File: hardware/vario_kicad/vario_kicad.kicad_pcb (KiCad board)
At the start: 2 copper layers, 70 x 50 mm, 94 parts, among them Q1 NMOS, Q2 PMOS, U2 BME280, U3 W25Q128JVS, U4 USB C connector, U5 STM32L072CBTx, Y1 Crystal, Y2 Crystal_GND24

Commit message: routing progress
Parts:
- R15, R4: moved to B.Cu
- moved C12 15.1 mm to (124.2, 135.8), turned to 180 degrees
- moved R26 12.8 mm to (124.1, 137.3), turned to 0 degrees
- moved C21 6.50 mm to (106.3, 139.9), turned to 180 degrees
- moved R15 2.86 mm to (113.0, 122.7)
- moved R4 2.02 mm to (112.5, 126.5)
- moved Y1 1.24 mm to (124.1, 130.3)
- moved C27 1.24 mm to (122.2, 128.9), turned to 90 degrees
- moved C26 1.11 mm to (122.2, 131.9), turned to -90 degrees
- moved R32 1.01 mm to (160.0, 135.2), turned to 180 degrees
- moved C13 0.06 mm to (133.2, 136.5)
- turned JP3 to 180 degrees
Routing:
- net V_USB: track 0.00 -> 78.4 mm, vias 0 -> 2
- net /mcu/NRST: track 0.00 -> 29.4 mm
- net /mcu/BOOT0: track 0.00 -> 22.6 mm
- net VBATT: track 0.00 -> 17.7 mm
- net /mcu/USB_D+: track 3.84 -> 18.4 mm
- net /mcu/USB_D-: track 3.36 -> 17.9 mm
- net /mcu/SWCLK: track 0.00 -> 13.5 mm
- net /mcu/SWDIO: track 0.00 -> 12.0 mm
- net VBATT_SW: track 0.00 -> 8.67 mm
- net Net-(U1-VoP): track 0.00 -> 8.33 mm
- net Net-(U1-VoN): track 0.00 -> 7.51 mm
- net Net-(Q1-D): track 0.00 -> 6.10 mm
- net /mcu/OSC32_OUT: track 0.00 -> 5.86 mm, vias 0 -> 1
- net /mcu/OSC32_IN: track 0.00 -> 5.61 mm, vias 0 -> 1
- net Net-(U4-CC1): track 0.03 -> 5.56 mm, vias 0 -> 1
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
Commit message: layout close to finished
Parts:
- C22: moved to B.Cu
- Y2: footprint Crystal:Crystal_SMD_3225-4Pin_3.2x2.5mm_HandSoldering -> Crystal:Crystal_SMD_3225-4Pin_3.2x2.5mm
- moved TP4 20.4 mm to (129.8, 137.8)
- moved D5 13.2 mm to (159.7, 135.4), turned to -90 degrees
- moved R28 12.9 mm to (158.2, 135.4), turned to -90 degrees
- moved C2 7.43 mm to (116.0, 111.1), turned to 90 degrees
- moved Q2 4.98 mm to (158.3, 127.1)
- moved R22 4.98 mm to (162.8, 126.1)
- moved R24 4.51 mm to (151.8, 127.7), turned to -90 degrees
- moved Q1 4.26 mm to (158.3, 131.7)
- moved R23 4.26 mm to (154.3, 131.7)
- moved R2 3.91 mm to (115.3, 117.0), turned to 180 degrees
- moved R25 3.55 mm to (149.8, 127.7)
- moved C1 2.91 mm to (110.9, 111.1), turned to 90 degrees
- moved R3 1.90 mm to (121.5, 112.0)
- moved C8 1.80 mm to (147.4, 114.6), turned to 180 degrees
- moved R5 1.40 mm to (121.4, 113.6)
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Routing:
- net VCC: track 3.17 -> 166.7 mm, vias 0 -> 12
- net GND: track 11.0 -> 77.4 mm, vias 0 -> 13
- net /mcu/SW3: track 0.00 -> 41.4 mm, vias 0 -> 2
- net /audio_amp/AUDIO_AMP_ENABLE: track 0.00 -> 34.0 mm, vias 0 -> 1
- net /mcu/MEM_CS_ALT: track 0.00 -> 31.9 mm, vias 0 -> 2
- net /leds/LED1: track 0.00 -> 29.8 mm
- net /leds/LED2: track 0.00 -> 27.3 mm
- net /mcu/ADC_IN3: track 0.00 -> 27.3 mm, vias 0 -> 1
- net /mcu/SPI1_NSS: track 0.00 -> 27.2 mm, vias 0 -> 2
- net /mcu/WKUP1: track 0.00 -> 26.5 mm
- net /leds/LED3: track 0.00 -> 24.9 mm
- net /bme280/BME280_I2C_SDA: track 0.00 -> 21.0 mm
- net /bme280/BME280_I2C_SCK: track 0.00 -> 20.7 mm, vias 0 -> 2
- net /mcu/SPI1_SCK: track 0.00 -> 18.8 mm
- net /mcu/MEM_HOLD: track 0.00 -> 18.7 mm, vias 0 -> 2
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- added copper zone on B.Cu, net GND

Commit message: layout&routing close to done
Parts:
- added C30: 100nF, Capacitor_SMD:C_0402_1005Metric, F.Cu at (128.5, 123.5)
- moved C12 15.2 mm to (112.0, 144.8), turned to -90 degrees
- moved R26 12.9 mm to (113.6, 144.8), turned to 90 degrees
- moved C1 3.30 mm to (107.6, 110.7)
- moved R1 3.30 mm to (107.0, 116.5)
- moved C2 3.30 mm to (112.8, 110.7)
- moved R2 3.30 mm to (112.0, 116.5)
- moved U2 3.30 mm to (110.2, 112.2)
- moved C29 1.03 mm to (116.0, 132.8)
- moved C25 0.94 mm to (130.8, 128.6)
- moved C11 0.94 mm to (132.2, 128.6)
- moved LS1 0.81 mm to (152.4, 115.5)
- moved C22 0.27 mm to (120.7, 122.0)
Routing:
- net /mcu/VBATT_SW_EN: track 0.00 -> 62.1 mm, vias 0 -> 1
- net VCC: track 166.7 -> 214.3 mm, vias 12 -> 14
- net /mcu/BOOT0: track 23.9 -> 4.57 mm
- net GND: track 77.4 -> 88.4 mm, vias 13 -> 20
- net VBATT: track 21.4 -> 28.5 mm
- net /mcu/SPI1_MOSI: track 16.3 -> 19.2 mm
- net Net-(JP3-A): track 3.59 -> 6.42 mm
- net /mcu/SPI1_NSS: track 27.2 -> 25.4 mm
- net /mcu/ADC_IN3: track 27.3 -> 29.1 mm, vias 1 -> 3
- net /bme280/BME280_I2C_SDA: track 21.0 -> 22.7 mm
- net /mcu/MEM_CS_ALT: track 31.9 -> 33.3 mm
- net /bme280/BME280_I2C_SCK: track 20.7 -> 22.1 mm
- net /mcu/SW3: track 41.4 -> 40.1 mm
- net Net-(U1-VoN): track 7.51 -> 8.56 mm
- net /mcu/MEM_WP: track 16.7 -> 17.7 mm
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- added copper zone on F.Cu, net GND

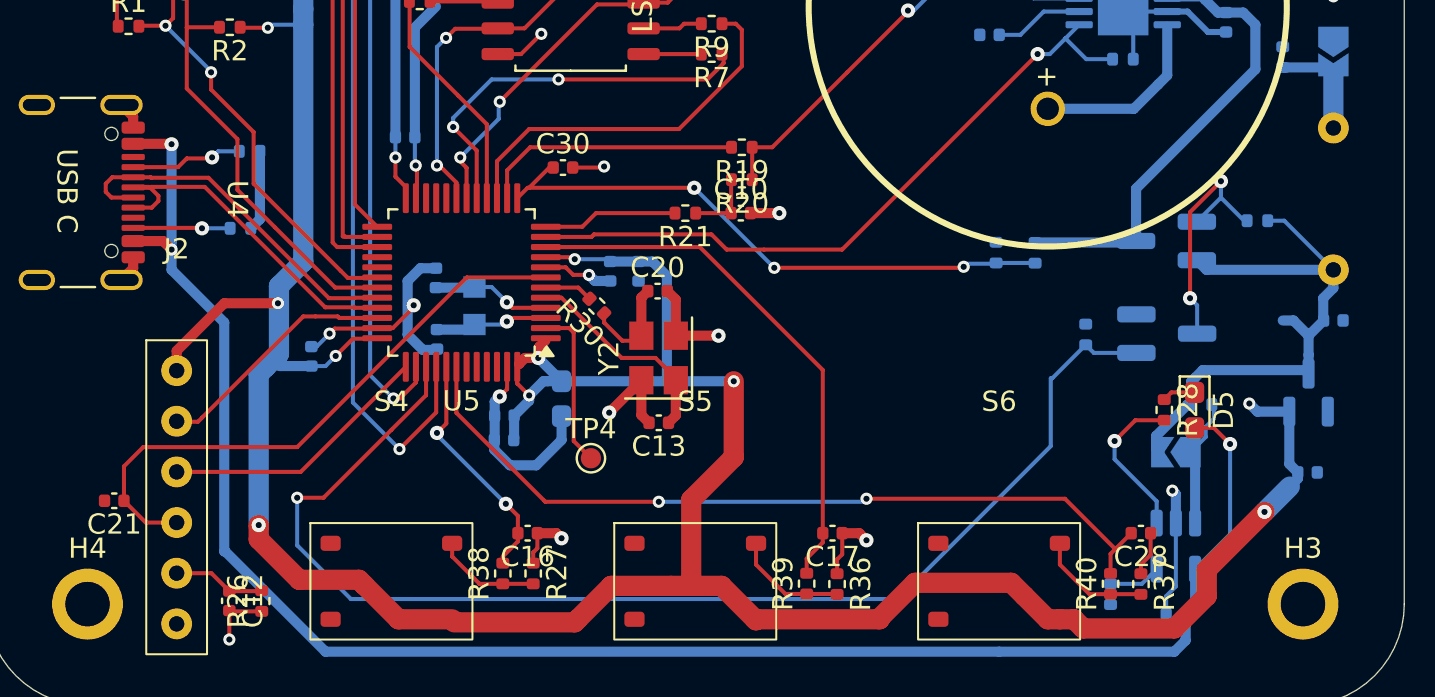
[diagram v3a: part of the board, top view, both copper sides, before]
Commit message: update usb c footprint for drc
shrink the usb c footprint pads closest to the NPTH mounting holes to
satisfy the DRC min distance 0.2mm hole to copper
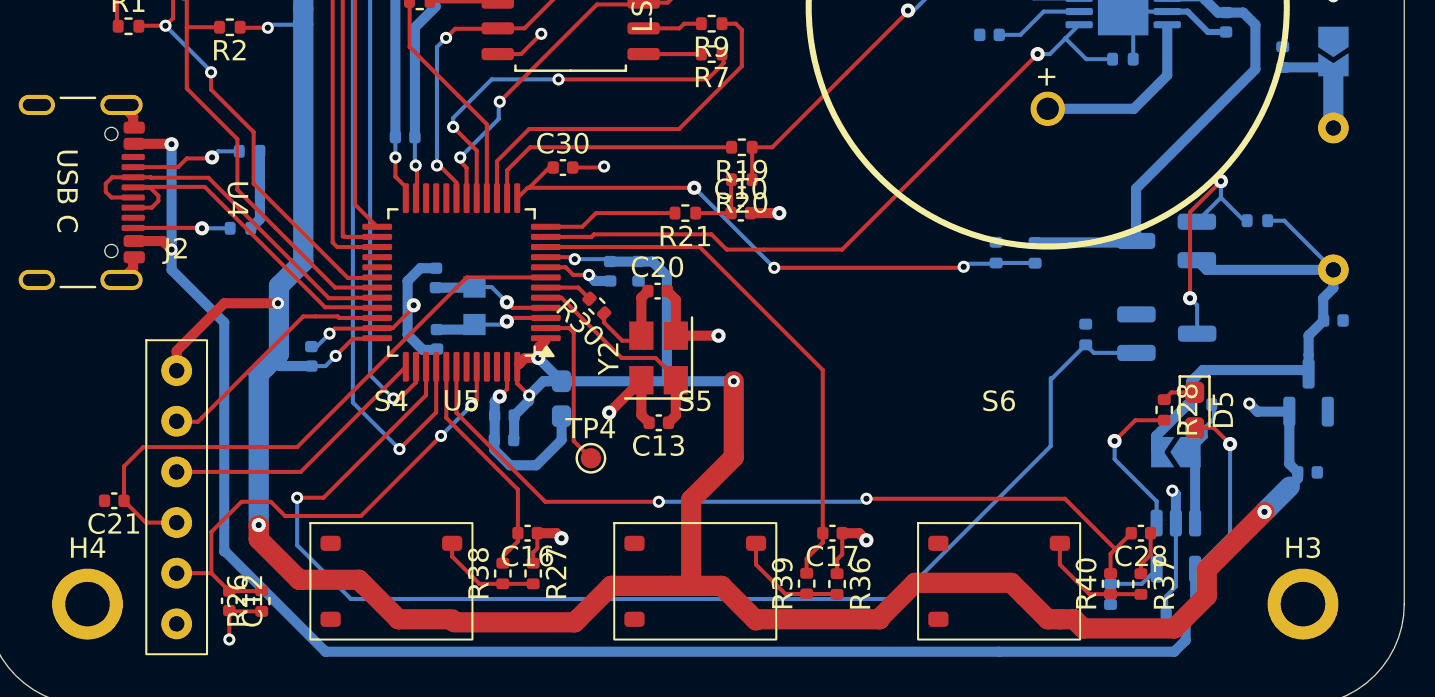
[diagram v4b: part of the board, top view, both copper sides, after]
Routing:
- net /mcu/BOOT0: track 4.57 -> 24.6 mm, vias 0 -> 2
- net VBATT: track 28.5 -> 26.9 mm
- net /mcu/SW1: track 11.8 -> 11.5 mm, vias 2 -> 0

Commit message: updates to layout v2
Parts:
- removed JP3: SolderJumper_2_Bridged, Jumper:SolderJumper-2_P1.3mm_Open_TrianglePad1.0x1.5mm
- BT2, C11, C22, C23, C24, C25, C29, C4, C8, C9, JP2, R15, R17, R18, R31, R4: moved to F.Cu
- C16, C17, C28, R27, R28, R36, R37, R38, R39, R40: moved to B.Cu
- moved R17 114.3 mm to (53.9, 53.9), turned to 0 degrees
- moved R18 112.5 mm to (53.9, 55.9), turned to 0 degrees
- moved R19 105.5 mm to (53.9, 57.8), turned to 0 degrees
- moved R20 105.3 mm to (53.9, 59.8), turned to 0 degrees
- moved C8 103.7 mm to (53.9, 69.7), turned to 0 degrees
- moved R21 102.9 mm to (53.9, 61.8), turned to 0 degrees
- moved C9 102.0 mm to (53.9, 71.7), turned to 0 degrees
- moved R26 101.0 mm to (74.2, 51.9), turned to 0 degrees
- moved TP4 98.9 mm to (58.9, 69.0)
- moved C10 98.3 mm to (53.9, 73.7)
- moved C11 95.3 mm to (62.9, 63.2), turned to 0 degrees
- moved C12 93.6 mm to (62.9, 65.2), turned to 0 degrees
- moved C23 92.5 mm to (65.8, 65.2), turned to 0 degrees
- moved C24 91.9 mm to (65.8, 67.2), turned to 0 degrees
- moved C25 88.1 mm to (65.8, 69.1), turned to 0 degrees
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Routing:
- net VCC: track 214.3 -> 7.95 mm, vias 14 -> 0
- net V_USB: track 87.6 -> 0.00 mm, vias 3 -> 0
- net GND: track 88.4 -> 5.75 mm, vias 20 -> 0
- net /mcu/VBATT_SW_EN: track 62.1 -> 0.00 mm, vias 1 -> 0
- net /mcu/SW3: track 40.1 -> 0.00 mm, vias 2 -> 0
- net /audio_amp/AUDIO_AMP_ENABLE: track 34.0 -> 0.00 mm, vias 1 -> 0
- net /mcu/MEM_CS_ALT: track 33.3 -> 0.00 mm, vias 2 -> 0
- net /leds/LED1: track 29.8 -> 0.00 mm
- net /mcu/NRST: track 29.4 -> 0.00 mm
- net /mcu/ADC_IN3: track 29.1 -> 0.00 mm, vias 3 -> 0
- net /leds/LED2: track 27.3 -> 0.00 mm
- net /mcu/WKUP1: track 26.5 -> 0.00 mm
- net /mcu/SPI1_NSS: track 25.4 -> 0.00 mm, vias 2 -> 0
- net /leds/LED3: track 24.9 -> 0.00 mm
- net /mcu/BOOT0: track 24.6 -> 0.00 mm, vias 2 -> 0
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
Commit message: update layout v2
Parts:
- C21, C23, C9, JP2, R18, R31: moved to B.Cu
- moved R17 111.4 mm to (139.1, 125.7), turned to 180 degrees
- moved R18 106.6 mm to (143.3, 114.0), turned to 180 degrees
- moved R19 104.0 mm to (135.5, 122.4), turned to 180 degrees
- moved R20 103.8 mm to (135.5, 124.0), turned to 180 degrees
- moved TP4 100.7 mm to (132.5, 137.7)
- moved C8 100.3 mm to (138.1, 124.1), turned to 180 degrees
- moved R21 99.8 mm to (131.9, 124.1), turned to 180 degrees
- moved C22 97.1 mm to (128.9, 136.9), turned to -90 degrees
- moved C11 96.8 mm to (131.9, 131.1), turned to -90 degrees
- moved C9 96.7 mm to (140.8, 114.0), turned to 180 degrees
- moved C10 95.3 mm to (133.6, 125.8), turned to -90 degrees
- moved C24 93.6 mm to (125.4, 139.3), turned to 180 degrees
- moved C25 89.3 mm to (130.1, 131.1), turned to -90 degrees
- moved C21 86.3 mm to (125.3, 130.7)
- moved C29 85.3 mm to (115.9, 136.2), turned to 135 degrees
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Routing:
- net VCC: track 7.95 -> 266.4 mm, vias 0 -> 11
- net V_USB: track 0.00 -> 100.5 mm, vias 0 -> 3
- net /leds/LED1: track 0.00 -> 41.8 mm
- net /leds/LED2: track 0.00 -> 38.9 mm
- net /mcu/MEM_CS_ALT: track 0.00 -> 37.1 mm, vias 0 -> 2
- net /leds/LED3: track 0.00 -> 35.9 mm
- net /audio_amp/AUDIO_AMP_ENABLE: track 0.00 -> 34.6 mm, vias 0 -> 1
- net /mcu/SW3: track 0.00 -> 33.4 mm, vias 0 -> 3
- net /mcu/VBATT_SW_EN: track 0.00 -> 33.3 mm, vias 0 -> 1
- net /mcu/SPI1_NSS: track 0.00 -> 31.7 mm, vias 0 -> 2
- net /bme280/BME280_I2C_SDA: track 0.00 -> 30.0 mm
- net VBATT_SW: track 0.00 -> 29.7 mm
- net GND: track 5.75 -> 35.3 mm, vias 0 -> 3
- net /bme280/BME280_I2C_SCK: track 0.00 -> 28.4 mm
- net /mcu/NRST: track 0.00 -> 25.0 mm, vias 0 -> 3
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
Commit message: almost finish 4layer board
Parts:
- removed C12: 100nF, Capacitor_SMD:C_0402_1005Metric
- C16, C17, C21, C23, C26, C27, C28, Q1, Q2, R22, R23, R24, R25, R27, R36, R37, R38, R39, R40, Y1: moved to F.Cu
- moved R26 100.4 mm to (114.5, 143.8), turned to 135 degrees
- moved C4 87.6 mm to (128.3, 138.0)
- moved C21 15.5 mm to (114.0, 141.3), turned to -45 degrees
- moved C27 14.4 mm to (133.4, 138.5), turned to -90 degrees
- moved R7 13.5 mm to (123.0, 125.8), turned to 90 degrees
- moved R9 13.5 mm to (124.5, 125.8), turned to 90 degrees
- moved R23 12.9 mm to (161.7, 138.0)
- moved C26 12.0 mm to (131.6, 138.5), turned to -90 degrees
- moved Y1 10.3 mm to (132.5, 136.2), turned to 180 degrees
- moved TP4 10.0 mm to (142.4, 139.2)
- moved C28 8.97 mm to (154.8, 143.0), turned to 90 degrees
- moved C17 8.61 mm to (141.8, 143.8), turned to 90 degrees
- moved R22 8.59 mm to (161.7, 133.9), turned to 90 degrees
- moved C16 8.01 mm to (129.3, 143.5), turned to 90 degrees
- moved R25 7.66 mm to (152.0, 130.9)
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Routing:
- net VCC: track 266.4 -> 49.2 mm, vias 11 -> 16
- net GND: track 35.3 -> 85.2 mm, vias 3 -> 35
- net /mcu/WKUP1: track 1.64 -> 20.9 mm, vias 0 -> 2
- net /mcu/SPI1_SCK: track 20.0 -> 2.42 mm
- net /mcu/RTC_CALIB: track 7.41 -> 24.6 mm, vias 0 -> 2
- net /mcu/SPI1_MOSI: track 19.3 -> 2.65 mm
- net Net-(U3-CLK): track 2.73 -> 15.5 mm
- net /mcu/VBATT_SW_EN: track 33.3 -> 45.3 mm, vias 1 -> 2
- net /mcu/MEM_CS_ALT: track 37.1 -> 26.9 mm
- net Net-(U3-DI(IO0)): track 2.71 -> 11.4 mm
- net V_USB: track 100.5 -> 92.3 mm
- net /audio_amp/AUDIO_AMP_ENABLE: track 34.6 -> 26.8 mm
- net /mcu/ADC_IN3: track 24.2 -> 30.9 mm, vias 3 -> 2
- net /leds/LED2: track 38.9 -> 32.5 mm
- net /leds/LED3: track 35.9 -> 30.0 mm
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- added copper zone on In1.Cu, net GND
- added copper zone on B.Cu, net VCC
- added copper zone on F.Cu, net VCC
- added copper zone on In2.Cu, net VCC
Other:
- copper layers 2 -> 4

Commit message: minor fixes
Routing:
- net VCC: vias 16 -> 15
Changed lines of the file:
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@@
 		(tags "resistor")
 		(property "Reference" "R37"
-			(at 0 -1.17 360)
+			(at 0 -1.17 0)
 			(layer "F.SilkS")
 			(hide yes)
@@
 		)
 		(property "Value" "100k"
-			(at 0 1.17 360)
+			(at 0 1.17 0)
 			(layer "F.Fab")
 			(effects
@@
 		)
 		(fp_text user "${REFERENCE}"
-			(at 0 0 360)
+			(at 0 0 0)
 			(layer "F.Fab")
 			(effects
@@
 		(tags "resistor")
 		(property "Reference" "R30"
-			(at 0 -1.17 360)
+			(at 0 -1.17 0)
 			(layer "F.SilkS")
 			(hide yes)
@@
 		)
 		(property "Value" "0R"
-			(at 0 1.17 360)
+			(at 0 1.17 0)
 			(layer "F.Fab")
 			(effects
@@
 		)
 		(fp_text user "${REFERENCE}"
-			(at 0 0 360)
+			(at 0 0 0)
 			(layer "F.Fab")
 			(effects
@@
 		(tags "capacitor")
 		(property "Reference" "C13"
-			(at 0 -1.16 360)
+			(at 0 -1.16 0)
 			(layer "F.SilkS")
 			(hide yes)
@@
 		)
 		(property "Value" "12.5pF"
-			(at 0 1.16 360)
+			(at 0 1.16 0)
 			(layer "F.Fab")
 			(effects
@@
 		)
 		(fp_text user "${REFERENCE}"
-			(at 0 0 360)
+			(at 0 0 0)
 			(layer "F.Fab")
 			(effects
@@
 		(tags "capacitor")
 		(property "Reference" "C20"
-			(at 0 -1.16 360)
+			(at 0 -1.16 0)
 			(layer "F.SilkS")
 			(hide yes)
@@
 		)
 		(property "Value" "12.5pF"
-			(at 0 1.16 360)
+			(at 0 1.16 0)
 			(layer "F.Fab")
 			(effects
@@
 		)
 		(fp_text user "${REFERENCE}"
-			(at 0 0 360)
+			(at 0 0 0)
 			(layer "F.Fab")
 			(effects
@@
 		(tags "SMD SMT crystal hand-soldering")
 		(property "Reference" "Y1"
-			(at 0 -1.8 360)
+			(at 0 -1.8 0)
 			(layer "F.SilkS")
 			(hide yes)
@@
 		)
 		(property "Value" "Crystal"
-			(at 0 1.8 360)
+			(at 0 1.8 0)
 			(layer "F.Fab")
 			(effects
@@
 		)
 		(fp_text user "${REFERENCE}"
-			(at 0 0 360)
+			(at 0 0 0)
 			(layer "F.Fab")
 			(effects
@@
 		(tags "SOT-23")
 		(property "Reference" "Q2"
-			(at 0 -2.75 360)
+			(at 0 -2.75 0)
 			(layer "F.SilkS")
 			(hide yes)
@@
 		)
 		(property "Value" "PMOS"
-			(at 0 2.5 360)
+			(at 0 2.5 0)
 			(layer "F.Fab")
 			(effects
@@
 		(attr smd)
 		(fp_line
-			(start -1.35 1.35)
-			(end -1.35 1.2)
-			(stroke
-				(width 0.1)
-				(type solid)
-			)
-			(layer "F.SilkS")
-		)
-		(fp_line
-			(start -1.35 1.36)
-			(end -1.2 1.36)
-			(stroke
-				(width 0.1)
-				(type solid)
-			)
-			(layer "F.SilkS")
-		)
-		(fp_line
-			(start 1.2 -1.35)
-			(end 1.35 -1.35)
-			(stroke
-				(width 0.1)
-				(type solid)
-			)
-			(layer "F.SilkS")
-		)
-		(fp_line
-			(start 1.35 -1.35)
-			(end 1.35 -1.2)
-			(stroke
-				(width 0.1)
-				(type solid)
-			)
-			(layer "F.SilkS")
-		)
-		(fp_line
-			(start 1.35 1.35)
-			(end 1.2 1.35)
+			(start -1.25 -0.5)
+			(end -1.25 0.5)
 			(stroke
 				(width 0.1)
-				(type solid)
+				(type default)
 			)
 			(layer "F.SilkS")
 		)
 		(fp_line
-			(start 1.35 1.35)
-			(end 1.35 1.2)
+			(start 1.25 -0.5)
+			(end 1.25 0.5)
 			(stroke
 				(width 0.1)
-				(type solid)
+				(type default)
 			)
 			(layer "F.SilkS")
@@
 	)
 	(via
-		(at 126.33 137.87)
-		(size 0.5)
-		(drill 0.3)
-		(layers "F.Cu" "B.Cu")
-		(free yes)
-		(net 3)
-	)
-	(via
 		(at 127.62 146.74)
 		(size 0.5)
@@
 		(start 120.42 111.68)
 		(end 120.42 112.93)
-		(width 0.1)
+		(width 0.2)
 		(layer "F.Cu")
 		(net 34)
@@
 		(start 122.75 110.31)
 		(end 122.74 110.3)
-		(width 0.1)
+		(width 0.2)
 		(layer "F.Cu")
 		(net 34)
@@
 		(start 120.42 112.93)
 		(end 120.41 112.94)
-		(width 0.1)
+		(width 0.2)
 		(layer "F.Cu")
 		(net 34)
@@
 	)
 	(segment
-		(start 123.76 126.98)
-		(end 123.76 124.29)
+		(start 123.77 126.82)
+		(end 123.77 124.3)
+		(width 0.2)
+		(layer "F.Cu")
+		(net 40)
+	)
+	(segment
+		(start 124.05 127.1)
+		(end 123.77 126.82)
 		(width 0.2)
 		(layer "F.Cu")
@@
 	(segment
 		(start 124.05 128.775)
-		(end 124.05 127.27)
+		(end 124.05 127.1)
 		(width 0.2)
 		(layer "F.Cu")
@@
 	)
 	(segment
-		(start 124.05 127.27)
-		(end 123.76 126.98)
+		(start 123.77 124.3)
+		(end 123.76 124.29)
 		(width 0.2)
 		(layer "F.Cu")
@@
 		(start 134.3 134.79)
 		(end 136.27 134.79)
-		(width 0.1)
+		(width 0.2)
 		(layer "F.Cu")
 		(net 59)
@@
 		(start 131.99 134.47)
 		(end 133.98 134.47)
-		(width 0.1)
+		(width 0.2)
 		(layer "F.Cu")
 		(net 59)
@@
 		(start 137.12 135.64)
 		(end 137.12 135.89)
-		(width 0.1)
+		(width 0.2)
 		(layer "F.Cu")
 		(net 59)
@@
 		(start 133.98 134.47)
 		(end 134.3 134.79)
-		(width 0.1)
+		(width 0.2)
 		(layer "F.Cu")
 		(net 59)
@@
 		(start 131.2075 133.6875)
 		(end 131.99 134.47)
-		(width 0.1)
+		(width 0.2)
 		(layer "F.Cu")
 		(net 59)
@@
 		(start 136.27 134.79)
 		(end 137.12 135.64)
-		(width 0.1)
+		(width 0.2)
 		(layer "F.Cu")
 		(net 59)
@@
 		(start 126.9625 133.6875)
 		(end 131.2075 133.6875)
-		(width 0.1)
+		(width 0.2)
 		(layer "F.Cu")
 		(net 59)
@@
 		(priority 2)
 		(connect_pads
-			(clearance 0.2)
+			(clearance 0.25)
 		)
 		(min_thickness 0.2)
@@
 			(clearance 0.2)
 		)
-		(min_thickness 0.25)
+		(min_thickness 0.2)
 		(filled_areas_thickness no)
 		(fill yes
 			(thermal_gap 0.5)
 			(thermal_bridge_width 0.5)
+			(smoothing fillet)
 		)
 		(polygon
@@
 		(name "GND input")
 		(hatch none 0.5)
-		(priority 3)
 		(connect_pads
-			(clearance 0.75)
+			(clearance 0.25)
 		)
 		(min_thickness 0.25)
@@
 		(name "VCC input")
 		(hatch none 0.5)
-		(priority 4)
 		(connect_pads
-			(clearance 0.75)
+			(clearance 0.25)
 		)
 		(min_thickness 0.25)
